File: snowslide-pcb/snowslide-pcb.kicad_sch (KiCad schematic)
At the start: 237 parts, among them J1 OLED, SW1 SW_Push, SW10 SW_Push, SW11 SW_Push, SW12 SW_Push, SW13 SW_Push, SW14 SW_Push, SW15 SW_Push, SW16 SW_Push, SW17 SW_Push, SW18 SW_Push, SW19 SW_Push, SW2 SW_Push, SW20 SW_Push, SW21 SW_Push, SW22 SW_Push, SW23 SW_Push, SW24 SW_Push, SW25 SW_Push, SW26 SW_Push, SW27 SW_Push, SW28 SW_Push, SW29 SW_Push, SW3 SW_Push, SW30 SW_Push, SW31 SW_Push, SW32 SW_Push, SW33 SW_Push, SW34 SW_Push, SW35 SW_Push, SW36 SW_Push, SW37 SW_Push, SW38 SW_Push, SW39 SW_Push, SW4 SW_Push, SW40 SW_Push, SW41 SW_Push, SW42 SW_Push, SW43 SW_Push, SW44 SW_Push, SW45 SW_Push, SW46 SW_Push, SW47 SW_Push, SW48 SW_Push, SW49 SW_Push, SW5 SW_Push, SW50 SW_Push, SW51 SW_Push, SW52 SW_Push, SW53 SW_Push, SW54 SW_Push, SW55 SW_Push, SW56 SW_Push, SW57 SW_Push, SW58 SW_Push, SW59 SW_Push, SW6 SW_Push, SW60 SW_Push, SW61 SW_Push, SW62 SW_Push, SW63 SW_Push, SW64 SW_Push, SW67 SW_Push, SW7 SW_Push, SW8 SW_Push, SW9 SW_Push, U1 Elite-C

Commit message: PCB layout completed.
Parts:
- removed JP1, JP2, JP3, JP4, JP5, JP6: Device_Jumper_NO_Small, used_footprints:Jumper_rev, symbol avalanche-hotswap:Device_Jumper_NO_Small
- D1, D10, D11, D12, D13, D14, D15, D16, D17, D18, D19, D2, D20, D21, D22, D23, D24, D25, D26, D27, D28, D29, D3, D30, D31, D32, D33, D34, D35, D36, D37, D38, D39, D4, D40, D41, D42, D43, D44, D45, D46, D47, D48, D49, D5, D50, D51, D52, D53, D54, D55, D56, D57, D58, D59, D6, D60, D61, D62, D63, D64, D7, D8, D9: footprint (none) -> footprints:D3_hybrid_common_hole_connected_fix
- ENC1, ENC2, ENC3, ENC4, ENC5, ENC6: footprint (none) -> footprints:RotaryEncoder_EC11
- H1, H2, HM1, HM10, HM11, HM12, HM13, HM14, HM15, HM16, HM17, HM18, HM19, HM2, HM20, HM21, HM22, HM23, HM24, HM25, HM26, HM27, HM28, HM3, HM4, HM5, HM6, HM7, HM8, HM9: footprint (none) -> footprints:spacer_m2
- SW1, SW10, SW11, SW12, SW13, SW14, SW15, SW16, SW17, SW18, SW19, SW2, SW20, SW21, SW22, SW23, SW24, SW25, SW26, SW27, SW28, SW29, SW3, SW30, SW31, SW32, SW33, SW34, SW35, SW36, SW37, SW38, SW39, SW4, SW40, SW41, SW42, SW43, SW44, SW45, SW46, SW47, SW48, SW49, SW5, SW50, SW51, SW52, SW53, SW54, SW55, SW56, SW57, SW58, SW59, SW6, SW60, SW61, SW62, SW63, SW64, SW7, SW8, SW9: footprint (none) -> footprints:CherryMX_Hotswap
- SW67: footprint (none) -> footprints:SW_Tactile_SPST_Angled_MJTP1117_fixed
- U1: footprint (none) -> footprints:Elite-C

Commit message: Checkpoint commit with merge from upstream.
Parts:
- J1: footprint used_footprints:OLED_4Pin_SSD1306 -> Connector_PinHeader_2.54mm:PinHeader_1x04_P2.54mm_Vertical
- L1, L10, L11, L12, L13, L14, L15, L16, L17, L18, L19, L2, L20, L21, L22, L23, L24, L25, L26, L27, L28, L29, L3, L30, L31, L32, L33, L34, L35, L36, L37, L38, L39, L4, L40, L41, L42, L43, L44, L45, L46, L47, L48, L49, L5, L50, L51, L52, L53, L54, L55, L56, L57, L58, L59, L6, L60, L61, L62, L63, L64, L7, L8, L9: footprint used_footprints:YS-SK6812MINI-E -> footprints:YS-SK6812MINI-E
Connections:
- net col0: now also SW27.2
- net row2: now also D14.1 (K), D15.1 (K), D16.1 (K), D17.1 (K), D18.1 (K), D19.1 (K)

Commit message: Checkpoint commit.
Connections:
- net GND: now also L1.3 (VSS), L10.3 (VSS), L2.3 (VSS), L3.3 (VSS), L36.3 (VSS), L4.3 (VSS), L5.3 (VSS), L6.3 (VSS), L7.3 (VSS), L8.3 (VSS), L9.3 (VSS)
- net VCC: now also L10.1 (VDD), L59.1 (VDD)
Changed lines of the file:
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@@
   (junction (at 260.604 21.59) (diameter 0) (color 0 0 0 0)
   )
+  (junction (at 153.67 188.595) (diameter 0) (color 0 0 0 0)
+  )
   (junction (at 178.435 22.86) (diameter 0) (color 0 0 0 0)
   )
@@
   (junction (at 227.838 163.195) (diameter 0) (color 0 0 0 0)
   )
+  (junction (at 40.132 110.49) (diameter 0) (color 0 0 0 0)
+  )
   (junction (at 162.814 221.107) (diameter 0) (color 0 0 0 0)
   )
@@
   (junction (at 199.898 43.18) (diameter 0) (color 0 0 0 0)
   )
+  (junction (at 111.125 220.98) (diameter 0) (color 0 0 0 0)
+  )
   (junction (at 164.084 149.987) (diameter 0) (color 0 0 0 0)
   )
@@
   (junction (at 153.035 68.58) (diameter 0) (color 0 0 0 0)
   )
-  (junction (at 146.939 153.67) (diameter 0) (color 0 0 0 0)
-  )
   (junction (at 117.475 53.34) (diameter 0) (color 0 0 0 0)
   )
@@
     (stroke (width 0) (type default) (color 0 0 0 0))
   )
+  (wire (pts (xy 111.125 220.98) (xy 128.524 221.107))
+    (stroke (width 0) (type default) (color 0 0 0 0))
+  )
   (wire (pts (xy 72.39 158.75) (xy 73.533 158.75))
     (stroke (width 0) (type default) (color 0 0 0 0))
@@
     (stroke (width 0) (type default) (color 0 0 0 0))
   )
-  (wire (pts (xy 42.291 110.49) (xy 41.91 110.49))
-    (stroke (width 0) (type default) (color 0 0 0 0))
-  )
   (wire (pts (xy 155.575 135.89) (xy 155.575 130.81))
     (stroke (width 0) (type default) (color 0 0 0 0))
@@
     (stroke (width 0) (type default) (color 0 0 0 0))
   )
+  (wire (pts (xy 40.005 110.49) (xy 40.132 110.49))
+    (stroke (width 0) (type default) (color 0 0 0 0))
+  )
   (wire (pts (xy 129.794 149.987) (xy 146.939 149.987))
     (stroke (width 0) (type default) (color 0 0 0 0))
@@
     (stroke (width 0) (type default) (color 0 0 0 0))
   )
-  (wire (pts (xy 207.772 120.015) (xy 213.741 120.015))
+  (wire (pts (xy 207.772 120.015) (xy 215.9 120.015))
     (stroke (width 0) (type default) (color 0 0 0 0))
   )
@@
     (stroke (width 0) (type default) (color 0 0 0 0))
   )
+  (wire (pts (xy 152.146 184.15) (xy 153.67 184.15))
+    (stroke (width 0) (type default) (color 0 0 0 0))
+  )
   (wire (pts (xy 117.475 21.59) (xy 117.475 22.86))
     (stroke (width 0) (type default) (color 0 0 0 0))
@@
     (stroke (width 0) (type default) (color 0 0 0 0))
   )
+  (wire (pts (xy 153.67 188.595) (xy 170.688 188.595))
+    (stroke (width 0) (type default) (color 0 0 0 0))
+  )
   (wire (pts (xy 123.698 229.87) (xy 123.698 234.315))
     (stroke (width 0) (type default) (color 0 0 0 0))
@@
     (stroke (width 0) (type default) (color 0 0 0 0))
   )
-  (wire (pts (xy 94.234 221.107) (xy 128.524 221.107))
+  (wire (pts (xy 94.234 221.107) (xy 111.125 220.98))
     (stroke (width 0) (type default) (color 0 0 0 0))
   )
@@
     (stroke (width 0) (type default) (color 0 0 0 0))
   )
+  (wire (pts (xy 153.67 184.15) (xy 153.67 188.595))
+    (stroke (width 0) (type default) (color 0 0 0 0))
+  )
   (wire (pts (xy 194.564 224.79) (xy 191.135 224.79))
     (stroke (width 0) (type default) (color 0 0 0 0))
@@
     (stroke (width 0) (type default) (color 0 0 0 0))
   )
+  (wire (pts (xy 111.125 220.98) (xy 111.125 224.79))
+    (stroke (width 0) (type default) (color 0 0 0 0))
+  )
   (wire (pts (xy 137.795 68.58) (xy 153.035 68.58))
     (stroke (width 0) (type default) (color 0 0 0 0))
@@
     (stroke (width 0) (type default) (color 0 0 0 0))
   )
-  (wire (pts (xy 146.939 153.67) (xy 146.939 167.132))
-    (stroke (width 0) (type default) (color 0 0 0 0))
-  )
   (wire (pts (xy 69.85 135.89) (xy 69.85 130.81))
     (stroke (width 0) (type default) (color 0 0 0 0))
@@
     (stroke (width 0) (type default) (color 0 0 0 0))
   )
+  (wire (pts (xy 40.132 110.49) (xy 41.91 110.49))
+    (stroke (width 0) (type default) (color 0 0 0 0))
+  )
   (wire (pts (xy 235.204 57.15) (xy 232.537 57.15))
     (stroke (width 0) (type default) (color 0 0 0 0))
@@
     (stroke (width 0) (type default) (color 0 0 0 0))
   )
-  (wire (pts (xy 152.146 184.15) (xy 153.543 184.15))
-    (stroke (width 0) (type default) (color 0 0 0 0))
-  )
   (wire (pts (xy 158.369 179.07) (xy 158.369 175.387))
     (stroke (width 0) (type default) (color 0 0 0 0))
@@
     (stroke (width 0) (type default) (color 0 0 0 0))
   )
-  (wire (pts (xy 136.398 188.595) (xy 170.688 188.595))
+  (wire (pts (xy 136.398 188.595) (xy 153.67 188.595))
     (stroke (width 0) (type default) (color 0 0 0 0))
   )
@@
     (stroke (width 0) (type default) (color 0 0 0 0))
   )
-  (wire (pts (xy 112.395 224.79) (xy 111.379 224.79))
+  (wire (pts (xy 111.125 224.79) (xy 112.395 224.79))
     (stroke (width 0) (type default) (color 0 0 0 0))
   )
@@
     (pin "1")
   )
-  (symbol (lib_id "power:GND") (at 215.138 120.015 180) (unit 1)
+  (symbol (lib_id "power:GND") (at 215.9 120.015 180) (unit 1)
     (in_bom yes) (on_board yes)
-    (property "Reference" "#PWR01" (id 0) (at 215.138 113.665 0)
+    (property "Reference" "#PWR01" (id 0) (at 215.9 113.665 0)
       (effects (font (size 1.27 1.27)) hide)
     )
-    (property "Value" "GND" (id 1) (at 215.138 117.221 90)
+    (property "Value" "GND" (id 1) (at 215.9 117.221 90)
       (effects (font (size 1.27 1.27)) (justify right))
     )
-    (property "Footprint" "" (id 2) (at 215.138 120.015 0)
+    (property "Footprint" "" (id 2) (at 215.9 120.015 0)
       (effects (font (size 1.27 1.27)) hide)
     )
-    (property "Datasheet" "" (id 3) (at 215.138 120.015 0)
+    (property "Datasheet" "" (id 3) (at 215.9 120.015 0)
       (effects (font (size 1.27 1.27)) hide)
     )

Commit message: Completed board and case.
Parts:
- removed ENC3, ENC6: Rotary_Encoder_Switch, footprints:RotaryEncoder_EC11, symbol avalanche-hotswap-rescue:Rotary_Encoder_Switch-Device
- removed H1, H2: MountingHole, footprints:spacer_m2, symbol Mechanical:MountingHole
- removed HM13, HM14, HM15, HM16, HM17, HM18, HM19, HM20, HM21, HM22, HM23, HM24, HM25, HM26, HM27, HM28, HM4: CaseHole, footprints:spacer_m2, symbol Mechanical:MountingHole
- removed L1, L10, L11, L12, L13, L14, L15, L16, L17, L18, L19, L2, L20, L21, L22, L23, L24, L25, L26, L27, L28, L29, L3, L30, L31, L32, L33, L34, L35, L36, L37, L38, L39, L4, L40, L41, L42, L43, L44, L45, L46, L47, L48, L49, L5, L50, L51, L52, L53, L54, L55, L56, L57, L58, L59, L6, L60, L61, L62, L63, L64, L7, L8, L9: SK6812MINI_LED, footprints:YS-SK6812MINI-E, symbol avalanche-hotswap:SK6812MINI_LED
- renumbered HM12 to HM4
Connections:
- net encA: no longer ENC4.A, ENC5.A
- net encB: no longer ENC4.B, ENC5.B
- net encC: now reaches U1.25 (B7)
- net encC: now also ENC4.A, ENC5.A
- net encD: now reaches U1.26 (D5)
- net encD: now also ENC4.B, ENC5.B
- no-connect marks 2 -> 0
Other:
- moved on the sheet: HM1, HM2, HM3, HM4, HM5, HM6

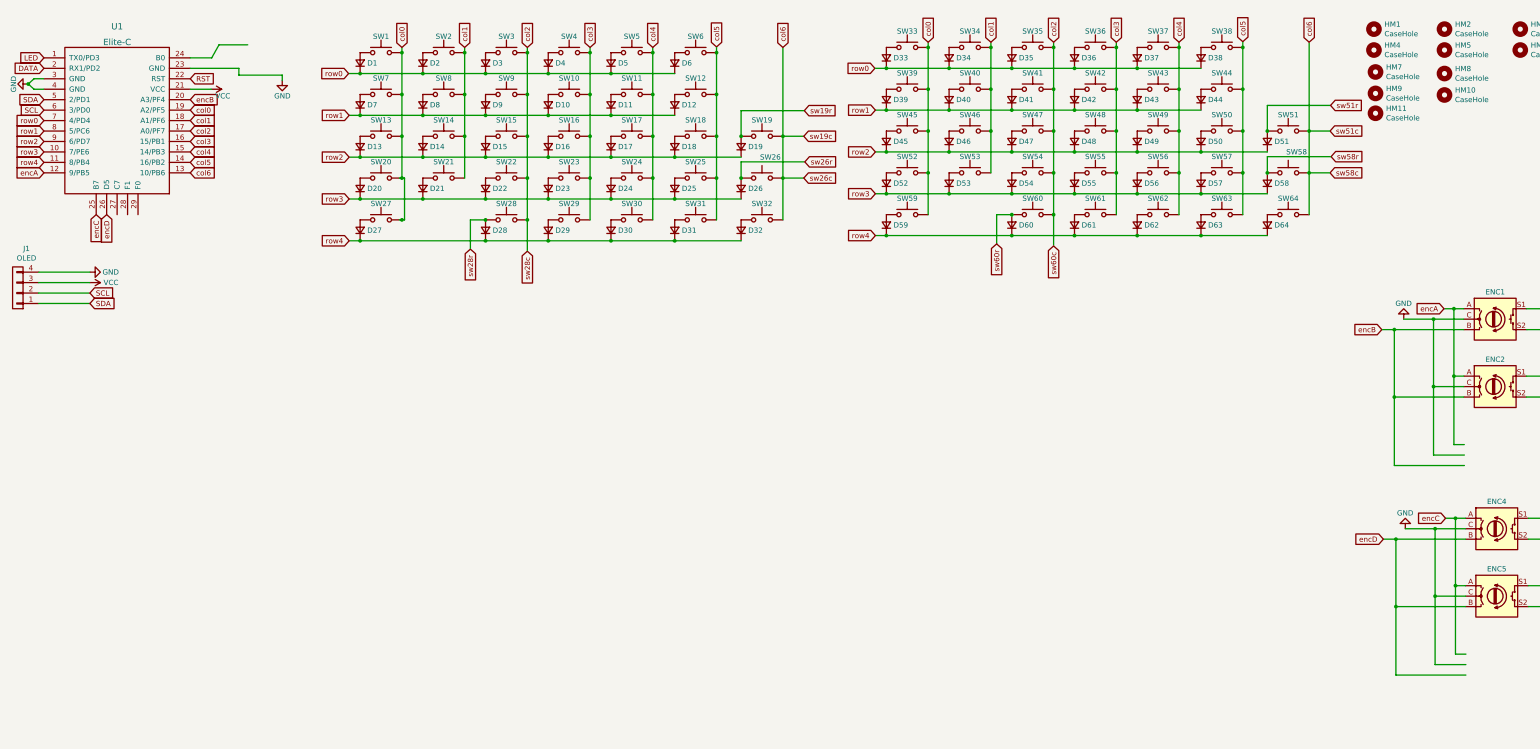
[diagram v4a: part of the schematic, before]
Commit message: Fixed schematic and PCB for horrible mistake with row connections.
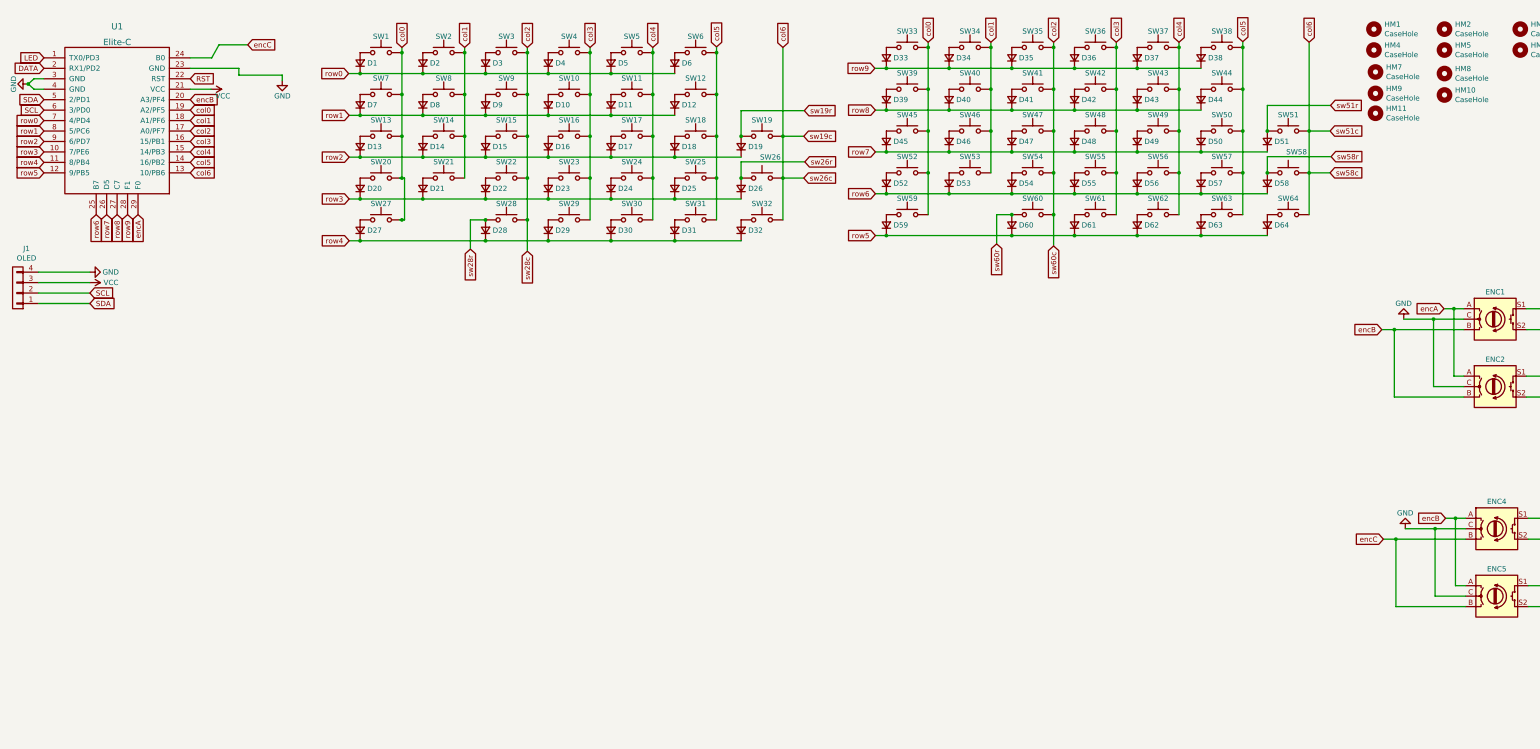
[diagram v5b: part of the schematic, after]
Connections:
- net encA: now also U1.29 (F0); no longer U1.12 (9/PB5)
- net encB: now also ENC4.A, ENC5.A
- net encC: now also ENC4.B, ENC5.B, U1.24 (B0); no longer ENC4.A, ENC5.A, U1.25 (B7)
- net row0: no longer D33.1 (K), D34.1 (K), D35.1 (K), D36.1 (K), D37.1 (K), D38.1 (K)
- net row1: no longer D39.1 (K), D40.1 (K), D41.1 (K), D42.1 (K), D43.1 (K), D44.1 (K)
- net row2: no longer D45.1 (K), D46.1 (K), D47.1 (K), D48.1 (K), D49.1 (K), D50.1 (K), D51.1 (K)
- net row3: no longer D52.1 (K), D53.1 (K), D54.1 (K), D55.1 (K), D56.1 (K), D57.1 (K), D58.1 (K)
- net row4: no longer D59.1 (K), D60.1 (K), D61.1 (K), D62.1 (K), D63.1 (K), D64.1 (K)
- net row8: now reaches U1.27 (C7)
- net row8: now also D39.1 (K), D40.1 (K), D41.1 (K), D42.1 (K), D43.1 (K), D44.1 (K)
- net row9: now reaches U1.28 (F1)
- net row9: now also D33.1 (K), D34.1 (K), D35.1 (K), D36.1 (K), D37.1 (K), D38.1 (K)
- removed net encD: ENC4.B, ENC5.B, U1.26 (D5)
- new net row5: D59.1 (K), D60.1 (K), D61.1 (K), D62.1 (K), D63.1 (K), D64.1 (K), U1.12 (9/PB5)
- new net row6: D52.1 (K), D53.1 (K), D54.1 (K), D55.1 (K), D56.1 (K), D57.1 (K), D58.1 (K), U1.25 (B7)
- new net row7: D45.1 (K), D46.1 (K), D47.1 (K), D48.1 (K), D49.1 (K), D50.1 (K), D51.1 (K), U1.26 (D5)

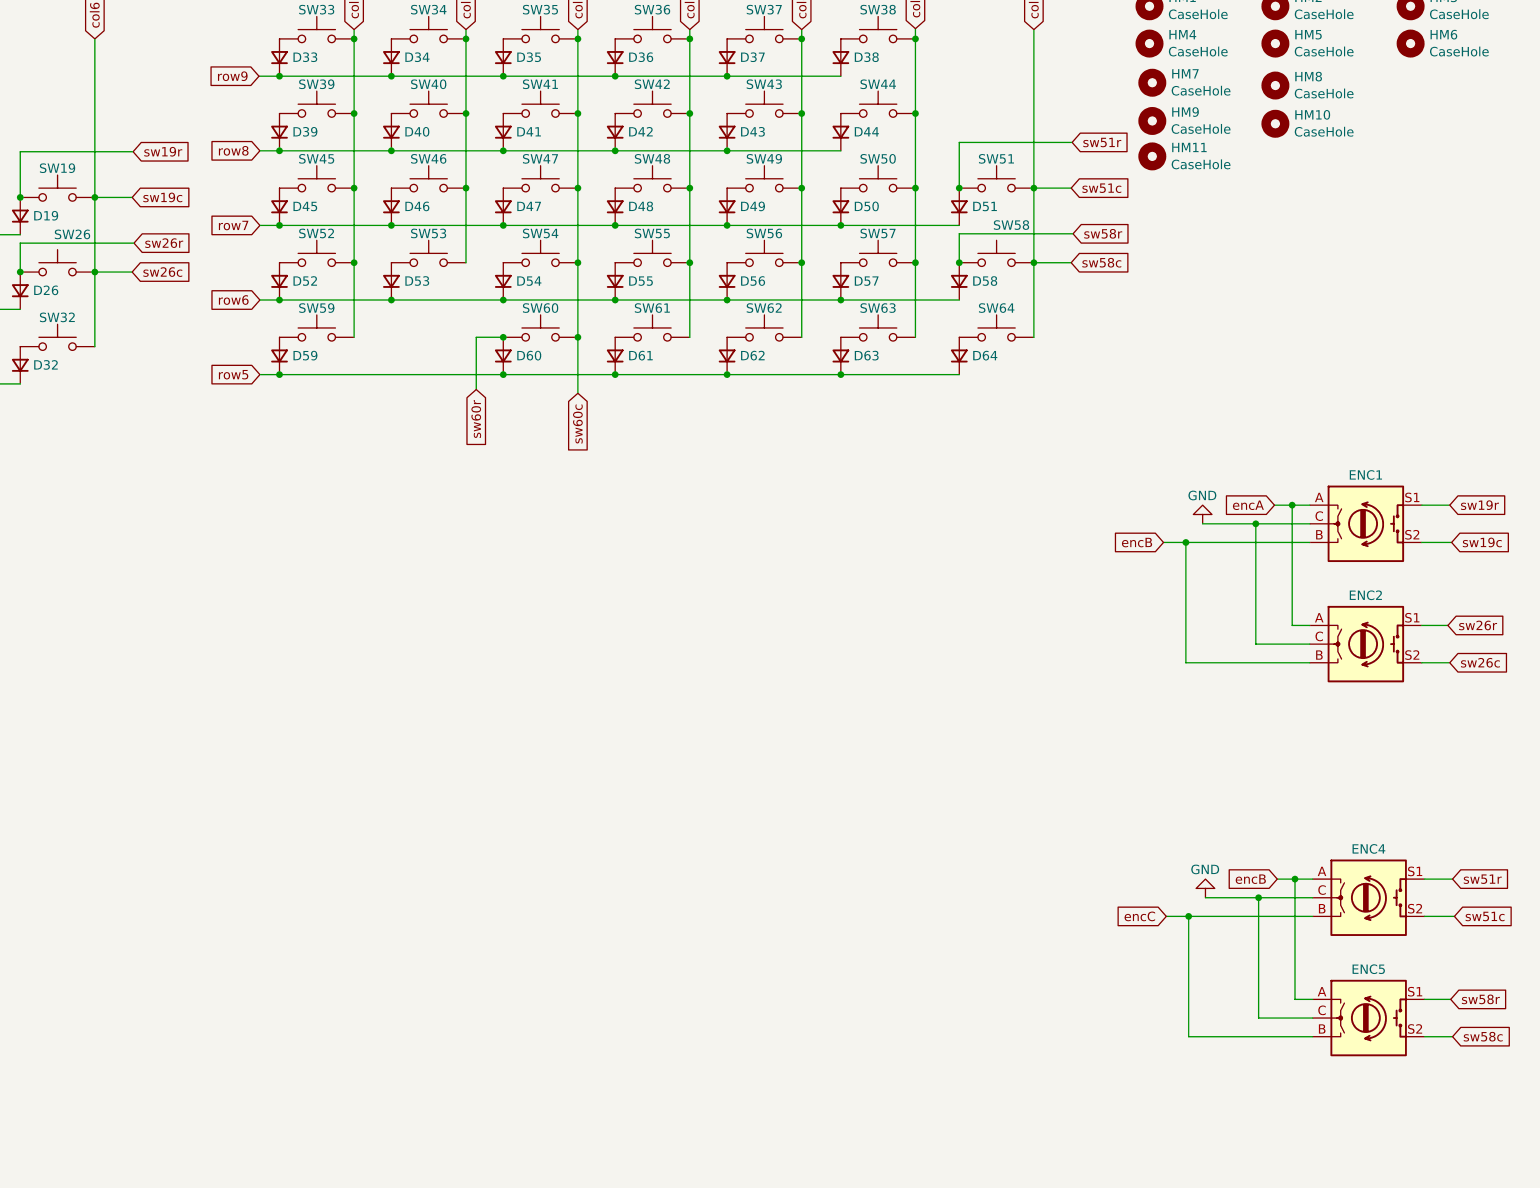
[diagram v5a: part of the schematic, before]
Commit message: Modded the board to have no encoders.
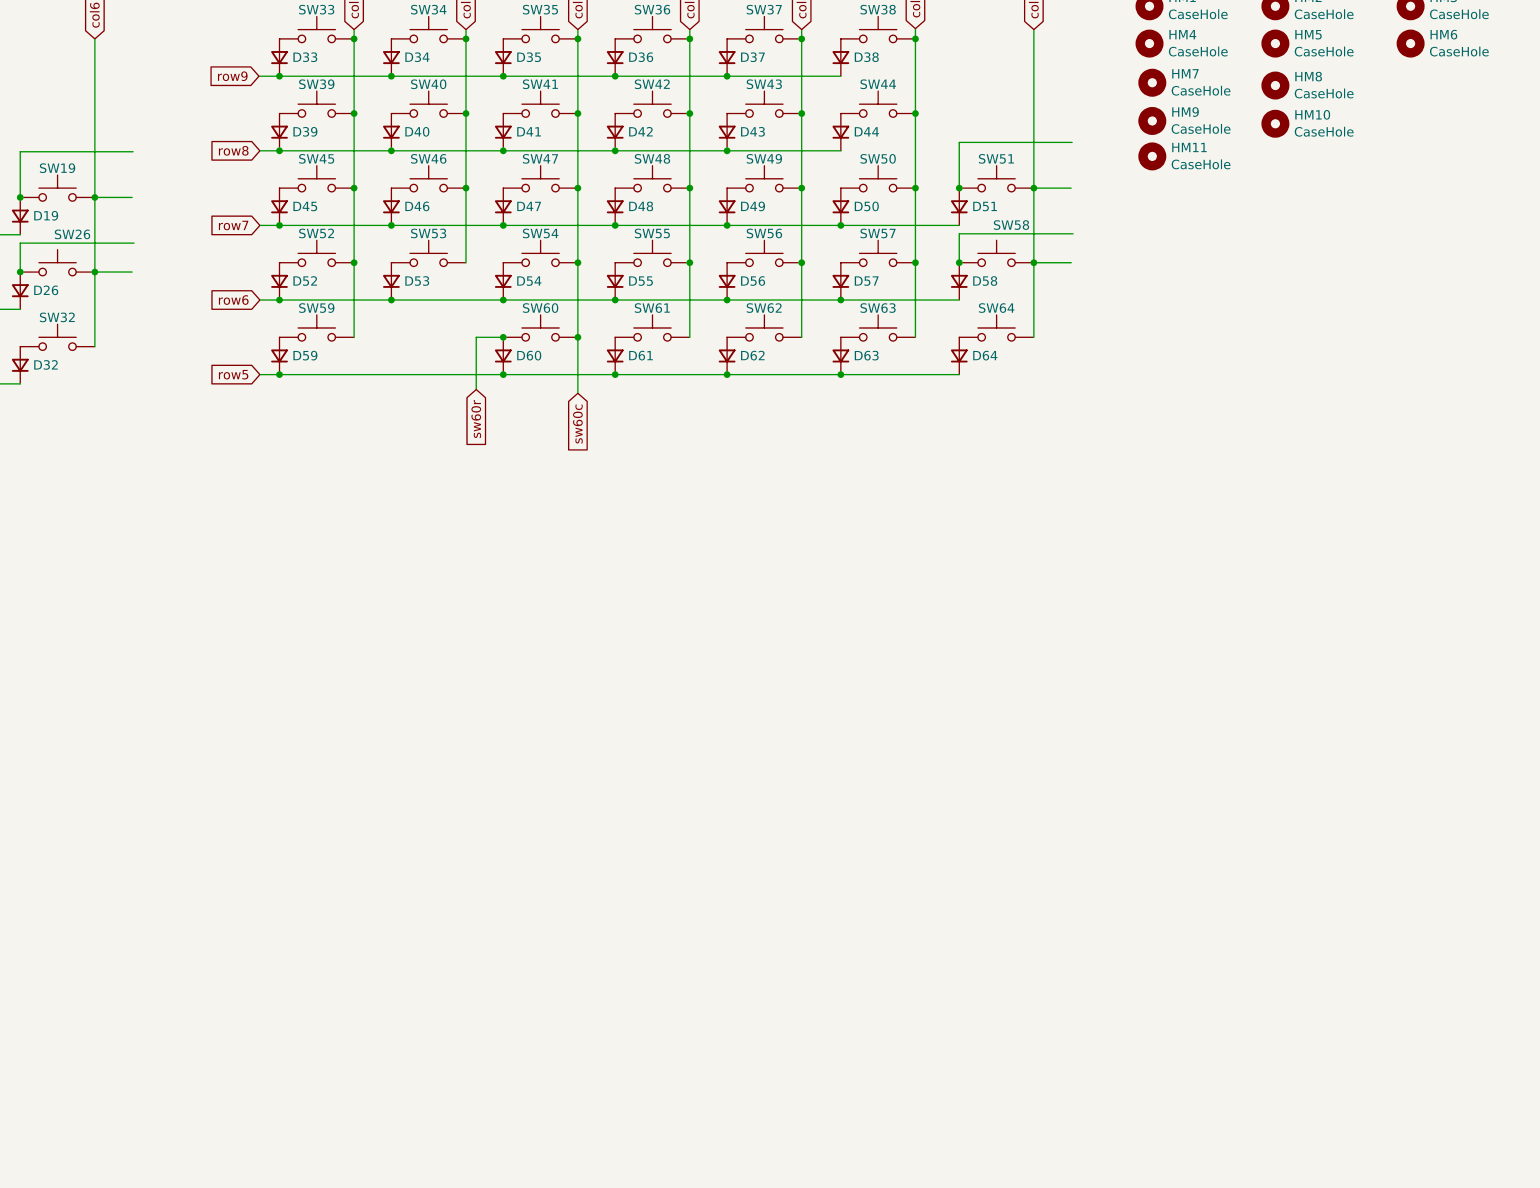
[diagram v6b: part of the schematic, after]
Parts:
- removed ENC1, ENC2, ENC4, ENC5: Rotary_Encoder_Switch, footprints:RotaryEncoder_EC11, symbol avalanche-hotswap-rescue:Rotary_Encoder_Switch-Device
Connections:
- net sw19r: no longer names the net of D19.2 (A), SW19.1
- net sw26r: no longer names the net of D26.2 (A), SW26.1
- net sw51r: no longer names the net of D51.2 (A), SW51.1
- net sw58r: no longer names the net of D58.2 (A), SW58.1
